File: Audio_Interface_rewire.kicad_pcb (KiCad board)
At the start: 2 copper layers, 72 x 92 mm, 62 parts, among them IC1 REG103GA-3.3_2K5, IC2 PCM2906CDB, IC3 INA849DGKT, J1 USB_B_Micro, J2 SJ-435107RS, J3 Vol. knob1 22k, J4 Vol. knob2 22k, J5 External Mic Conn., Q1 J304, SW1 HID0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

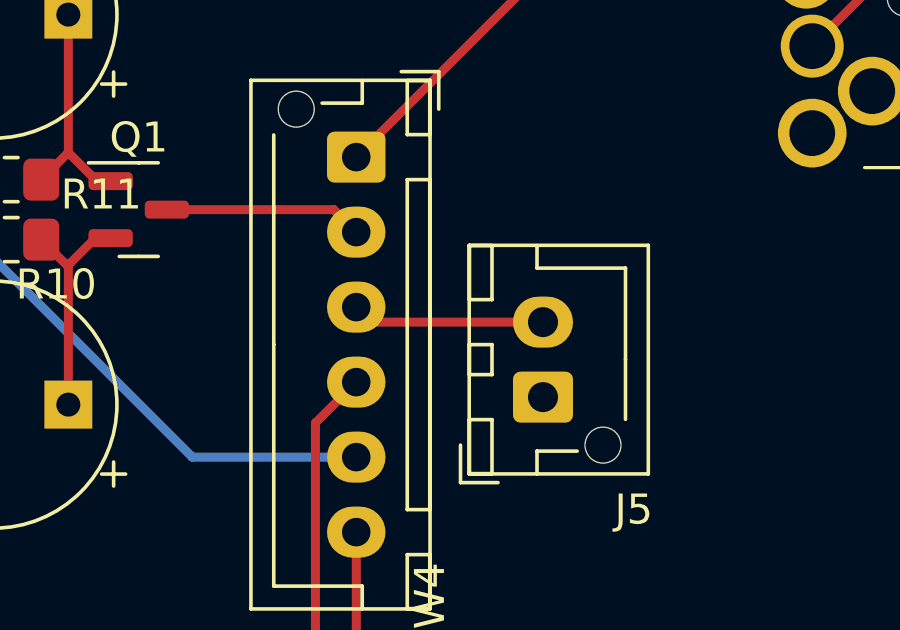
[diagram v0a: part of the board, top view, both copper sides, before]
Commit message: Changed microphone input system
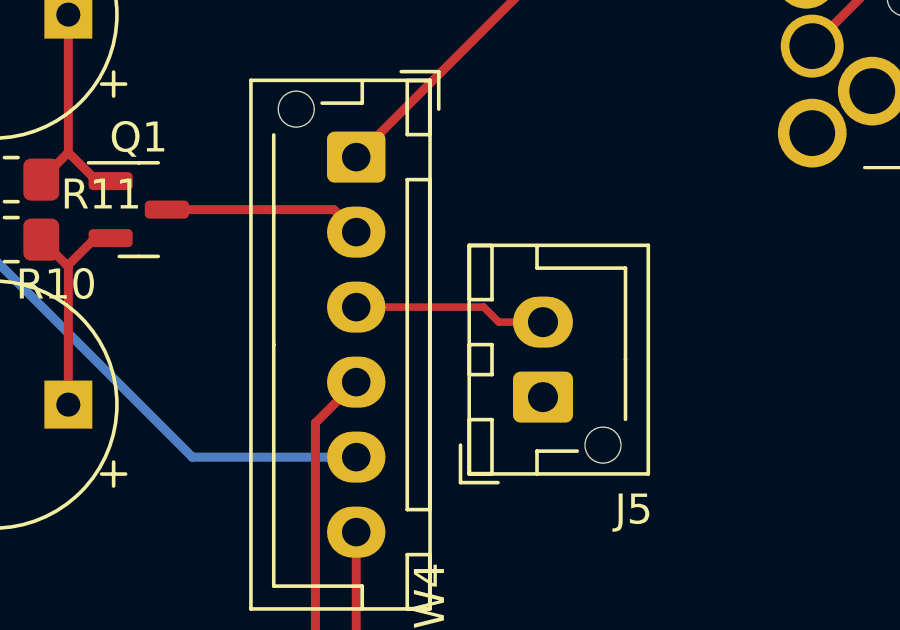
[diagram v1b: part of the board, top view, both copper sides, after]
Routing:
- net /External mic: track 6.43 -> 7.14 mm
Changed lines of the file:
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@@
   (segment (start 109.7355 161.2645) (end 110.5 160.5) (width 0.3) (layer "F.Cu") (net 43))
   (segment (start 105.9 161.2645) (end 109.7355 161.2645) (width 0.3) (layer "F.Cu") (net 43))
+  (segment (start 134.25 144.75) (end 134.75 145.25) (width 0.25) (layer "F.Cu") (net 44))
   (segment (start 130.5 145.25) (end 130 144.75) (width 0.3) (layer "F.Cu") (net 44))
-  (segment (start 136.225 145.25) (end 130.5 145.25) (width 0.3) (layer "F.Cu") (net 44))
+  (segment (start 134.75 145.25) (end 136.225 145.25) (width 0.25) (layer "F.Cu") (net 44))
+  (segment (start 130 144.75) (end 134.25 144.75) (width 0.25) (layer "F.Cu") (net 44))
   (segment (start 96 102) (end 99.25 102) (width 0.3) (layer "F.Cu") (net 45))
   (segment (start 99.25 102) (end 100.25 103) (width 0.3) (layer "F.Cu") (net 45))

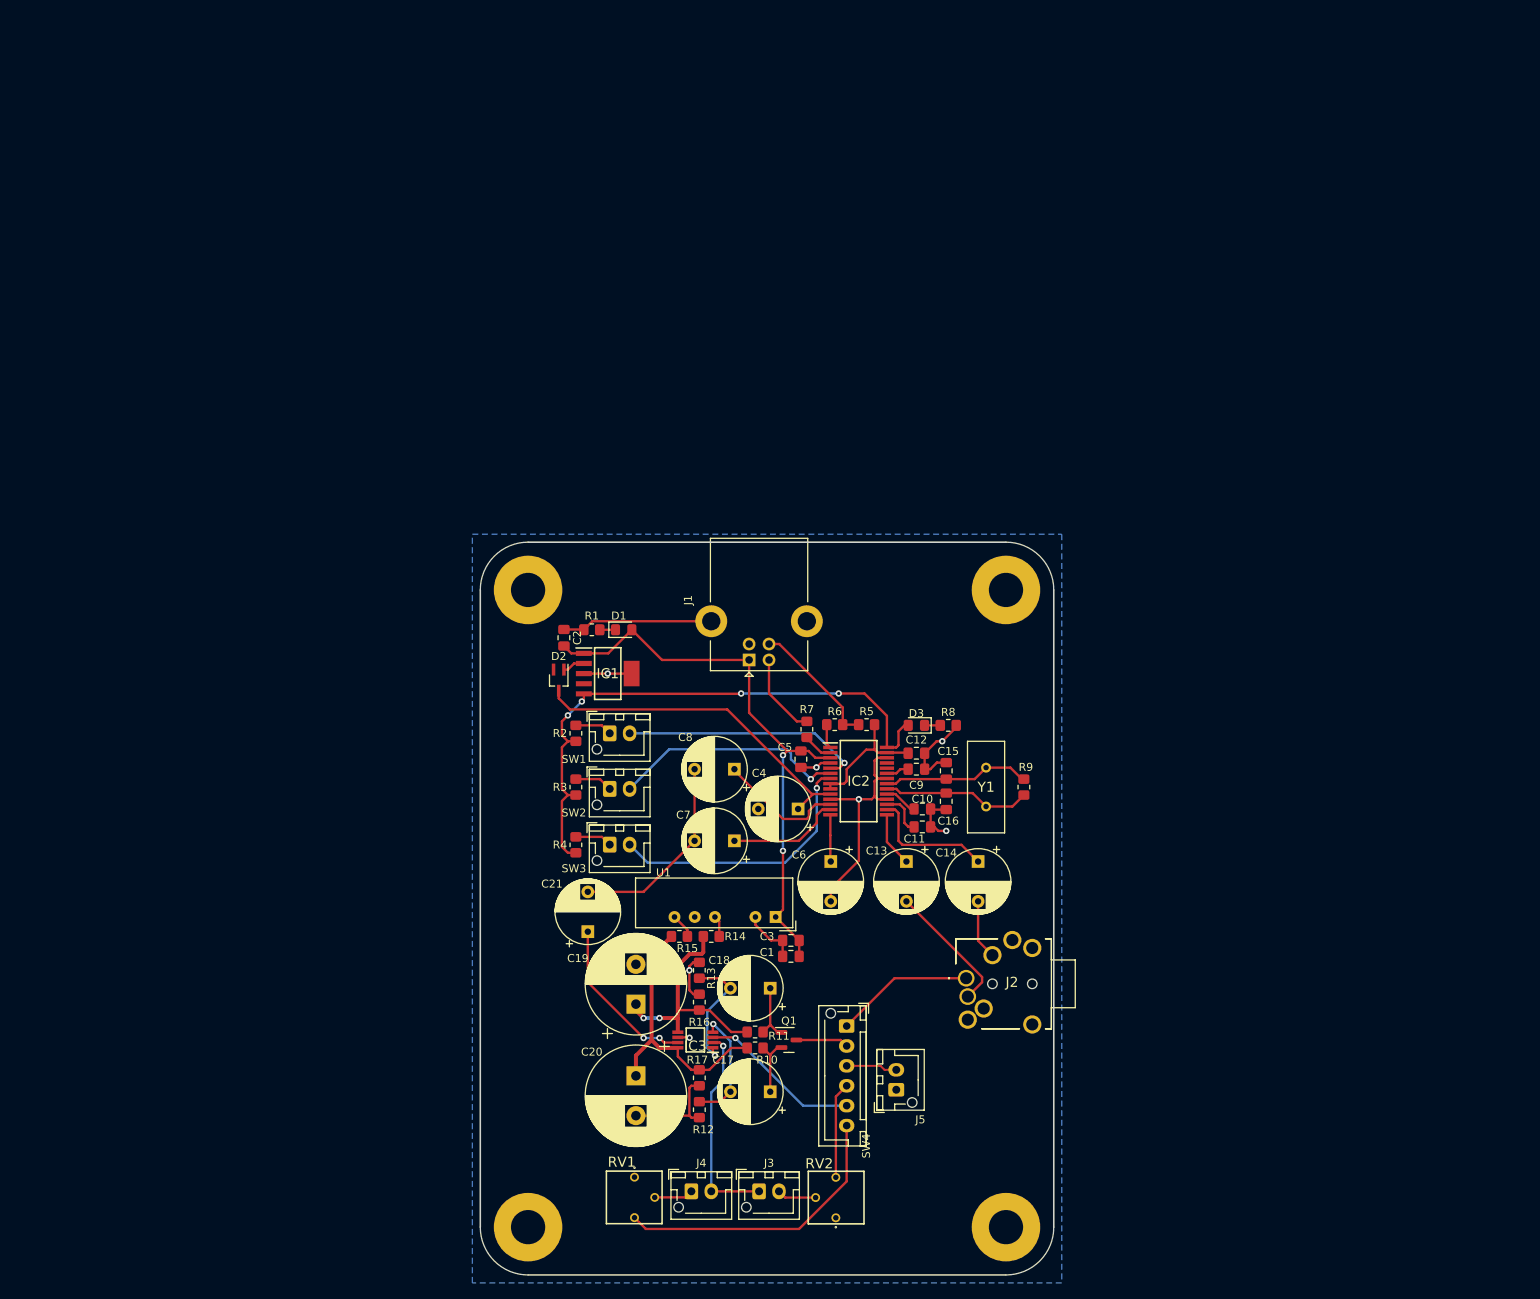
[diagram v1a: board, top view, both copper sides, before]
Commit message: started wiring the pcb
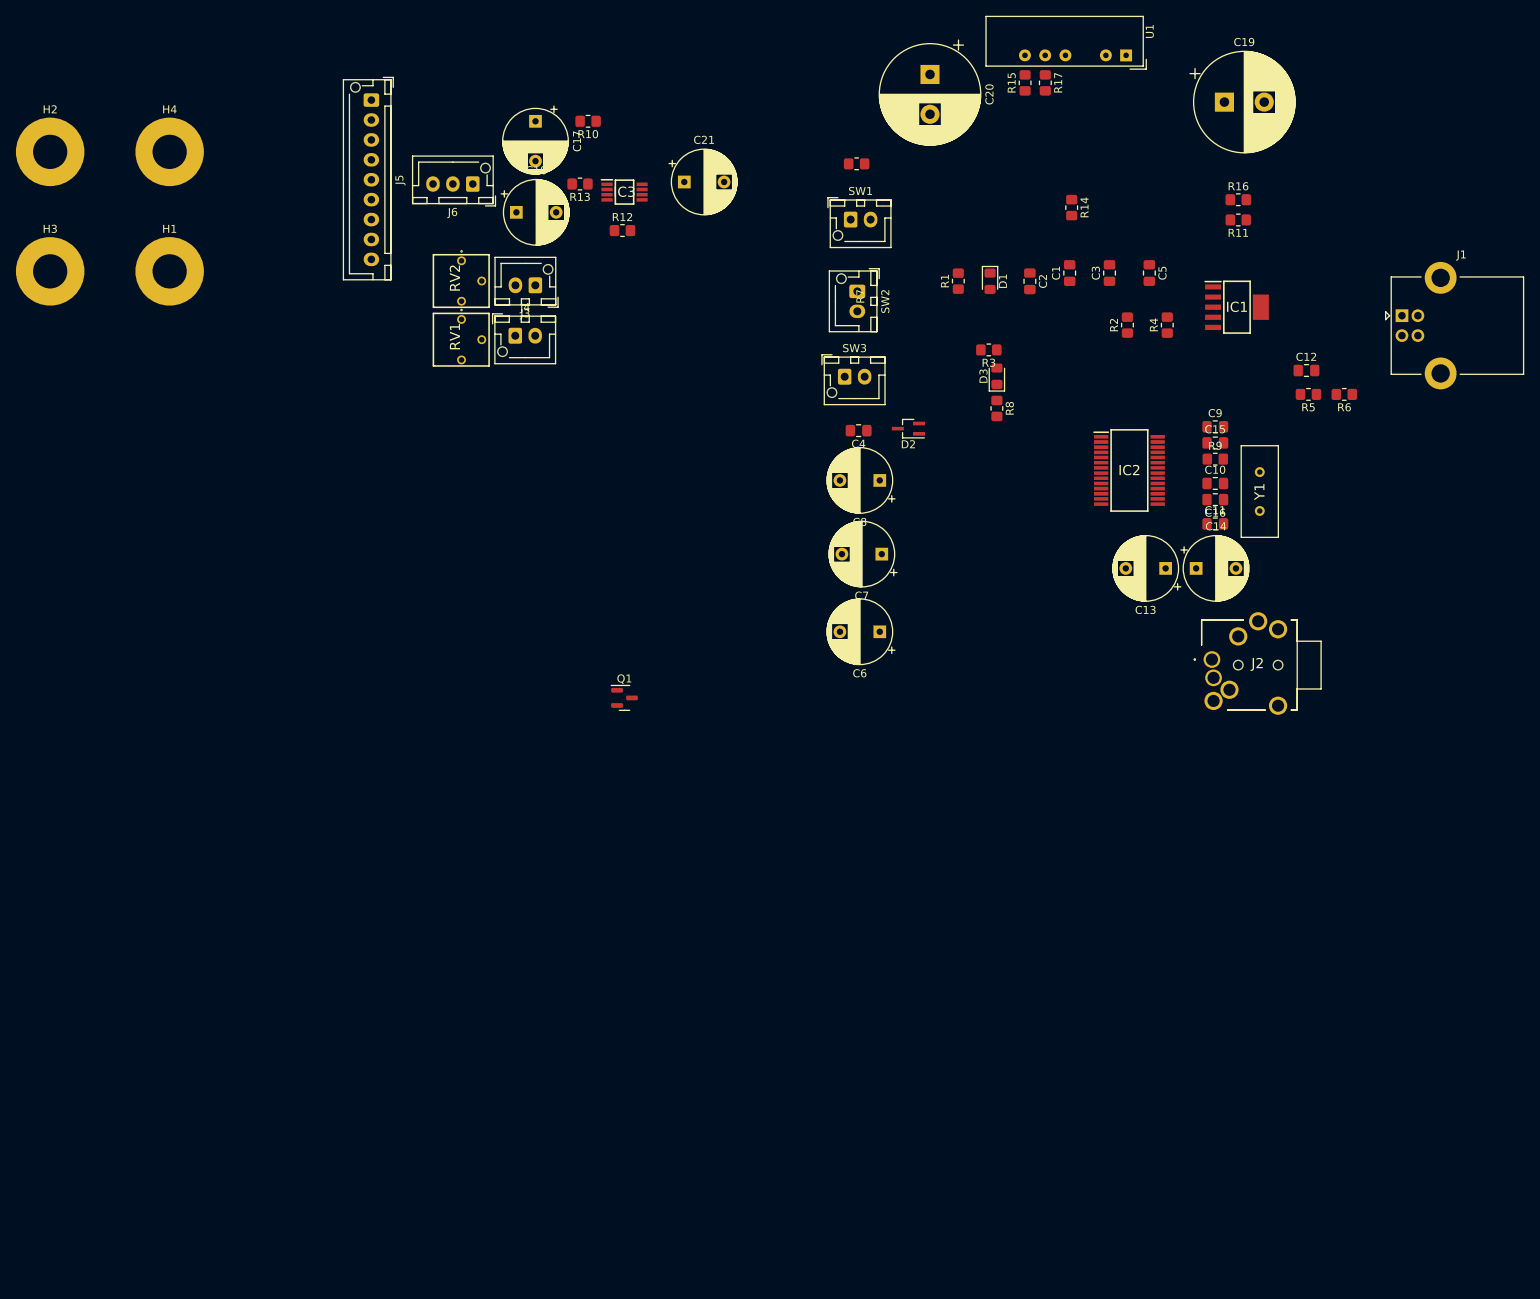
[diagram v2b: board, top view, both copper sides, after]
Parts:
- removed SW4: SW_Push_DPDT, Connector_JST:JST_XH_B6B-XH-AM_1x06_P2.50mm_Vertical
- added J6: External mic. conn., Connector_JST:JST_XH_B3B-XH-AM_1x03_P2.50mm_Vertical, F.Cu at (83.1, 34.0)
- C4: footprint Capacitor_THT:CP_Radial_D8.0mm_P5.00mm -> Capacitor_SMD:C_0805_2012Metric_Pad1.18x1.45mm_HandSolder
- IC2: footprint Package_SO:SOP65P780X200-28N -> IC_Downloaded:SOP65P780X200-28N
- J5: value External Mic Conn. -> SW_PUSH_3PDT; footprint Connector_JST:JST_XH_B2B-XH-AM_1x02_P2.50mm_Vertical -> Connector_JST:JST_XH_B9B-XH-AM_1x09_P2.50mm_Vertical
- moved H4 171.0 mm to (45.0, 30.0)
- moved H2 147.7 mm to (30.0, 30.0)
- moved J5 140.6 mm to (70.3, 23.5), turned to -90 degrees
- moved C19 135.2 mm to (177.4, 23.8), turned to 0 degrees
- moved R17 132.3 mm to (154.9, 21.3)
- moved C20 131.0 mm to (140.5, 20.3)
- moved RV2 127.1 mm to (78.1, 46.2), turned to -90 degrees
- moved H3 126.5 mm to (30.0, 45.0)
- moved C17 125.4 mm to (90.9, 26.2), turned to -90 degrees
- moved R16 121.4 mm to (179.2, 36.0), turned to 0 degrees
- moved R11 118.6 mm to (179.2, 38.5)
- moved R10 118.2 mm to (97.5, 26.2), turned to 180 degrees
- moved J3 117.2 mm to (90.9, 46.8), turned to 180 degrees
- moved U1 116.8 mm to (165.1, 17.9)
- moved R15 115.6 mm to (152.4, 21.3), turned to 90 degrees
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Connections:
- C17 pad 1: Net-(C17-Pad1) -> /V_IN_S
- C18 pad 1: Net-(C18-Pad1) -> /V_IN_D
- J5 pad 1: GND -> /hp_mic
- J5 pad 2: /External mic -> /RG_2
- Q1 pad 1: Net-(C18-Pad1) -> /INT_MIC_D
- Q1 pad 2: Net-(C17-Pad1) -> /INT_MIC_S
- Q1 pad 3: /V_IN -> /Headphones mic
- R10 pad 2: Net-(C17-Pad1) -> /V_IN_S
- R11 pad 1: Net-(C18-Pad1) -> /V_IN_D
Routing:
- net GND: track 104.4 -> 0.00 mm, vias 7 -> 0
- net /~{SSPND}: track 73.7 -> 0.00 mm, vias 4 -> 0
- net VBUS: track 73.2 -> 0.00 mm, vias 2 -> 0
- net Net-(C4-Pad1): track 42.7 -> 0.00 mm
- net /hp_mic: track 36.7 -> 0.00 mm
- net /+vs: track 34.7 -> 0.00 mm
- net /HID2: track 34.0 -> 0.00 mm, vias 1 -> 0
- net /-vs: track 30.6 -> 0.00 mm, vias 2 -> 0
- net /HID0: track 30.6 -> 0.00 mm, vias 1 -> 0
- net /HID1: track 29.6 -> 0.00 mm, vias 1 -> 0
- net /RG_1: track 26.3 -> 0.00 mm, vias 1 -> 0
- net /Audio_signal: track 25.1 -> 0.00 mm
- net Net-(C21-Pad1): track 20.8 -> 0.00 mm, vias 2 -> 0
- net /RG_2: track 20.4 -> 0.00 mm, vias 1 -> 0
- net /XTO_Crystal: track 18.7 -> 0.00 mm
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- removed copper zone on B.Cu, net GND
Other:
- board outline removed

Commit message: finished the pcb design
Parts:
- moved H3 180.2 mm to (189.8, 128.2)
- moved H4 150.5 mm to (189.8, 70.9)
- moved H2 118.5 mm to (96.4, 128.2)
- moved C19 106.1 mm to (136.6, 121.7)
- moved J5 100.0 mm to (99.2, 119.2), turned to 90 degrees
- moved R16 91.4 mm to (132.9, 114.8)
- moved R11 84.9 mm to (132.9, 109.7), turned to 0 degrees
- moved R14 79.9 mm to (132.9, 112.8), turned to 180 degrees
- moved C18 79.9 mm to (126.6, 107.8), turned to 90 degrees
- moved IC3 77.3 mm to (134.7, 105.2)
- moved J3 76.2 mm to (127.1, 113.8)
- moved J4 76.2 mm to (124.5, 120.1)
- moved RV1 76.2 mm to (114.3, 120.6)
- moved RV2 76.2 mm to (114.3, 113.3)
- moved R10 76.1 mm to (132.2, 94.0), turned to -90 degrees
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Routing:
- net GND: track 0.00 -> 172.3 mm, vias 0 -> 7
- net VBUS: track 0.00 -> 68.7 mm, vias 0 -> 2
- net /Headphones mic: track 0.00 -> 56.2 mm
- net /~{SSPND}: track 0.00 -> 47.6 mm
- net /INT_MIC_D: track 0.00 -> 42.6 mm, vias 0 -> 2
- net /V_IN_S: track 0.00 -> 40.8 mm, vias 0 -> 2
- net /RG_2: track 0.00 -> 39.5 mm, vias 0 -> 4
- net /V_IN_D: track 0.00 -> 36.1 mm, vias 0 -> 2
- net -15V: track 0.00 -> 31.6 mm
- net /+vs: track 0.00 -> 29.4 mm
- net /HID2: track 0.00 -> 27.9 mm
- net /XTO_Crystal: track 0.00 -> 25.7 mm, vias 0 -> 2
- net /RG_1: track 0.00 -> 23.8 mm
- net /hp_mic: track 0.00 -> 20.3 mm
- net /EXT_MIC_S: track 0.00 -> 20.2 mm, vias 0 -> 2
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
